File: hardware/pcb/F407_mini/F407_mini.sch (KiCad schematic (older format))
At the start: 37 parts, among them J1 Conn_01x03, J10 Conn_01x03, J11 Conn_01x03, J12 Conn_01x03, J13 Conn_01x03, J14 Conn_01x03, J15 Conn_01x03, J16 Conn_01x03, J17 Conn_01x03, J18 Conn_01x03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

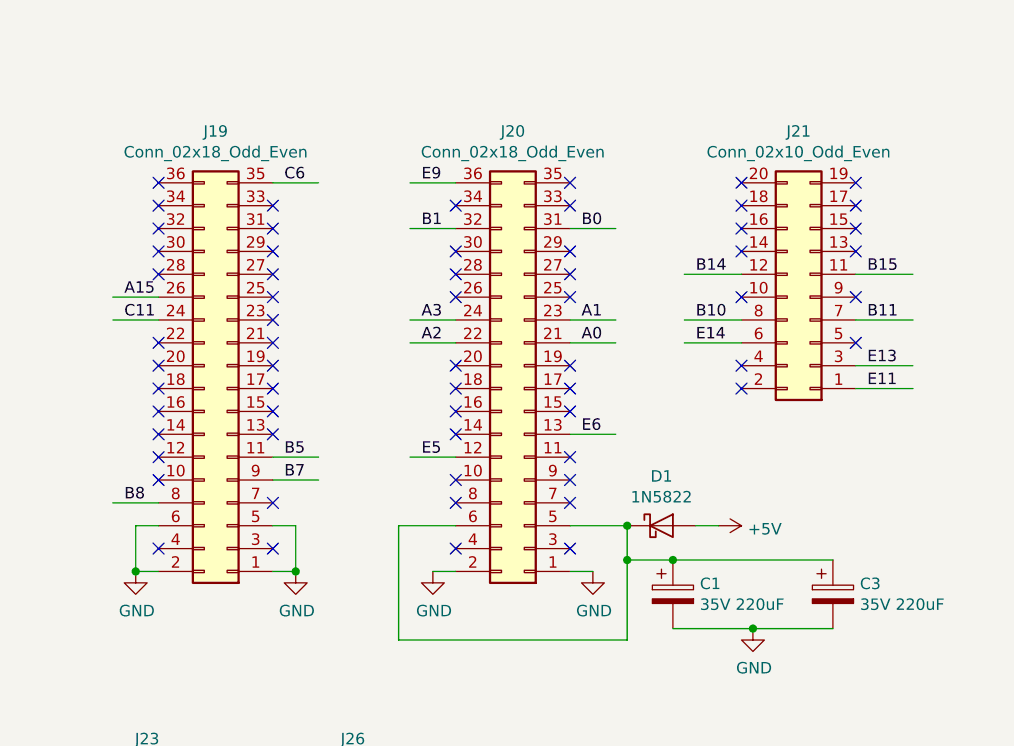
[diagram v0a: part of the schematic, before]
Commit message: flip connectors
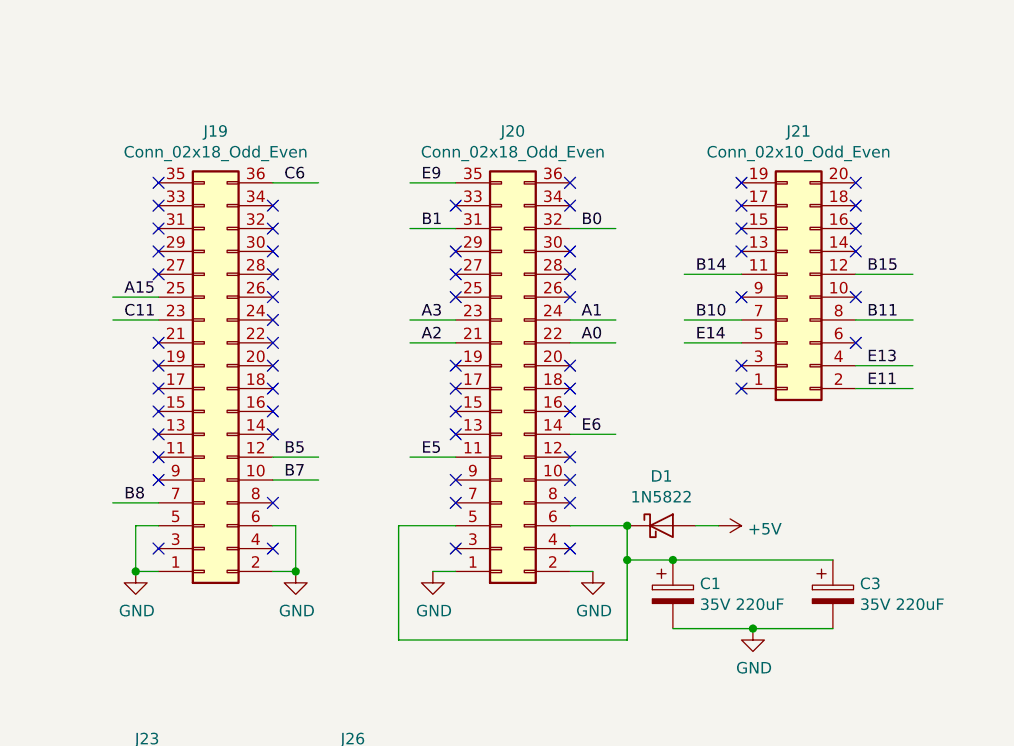
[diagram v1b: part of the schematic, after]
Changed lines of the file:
@@
 L Connector_Generic:Conn_02x10_Odd_Even J21
 U 1 1 5E1B89D1
-P 10000 1950
-F 0 "J21" H 10050 1225 50  0000 C CNN
-F 1 "Conn_02x10_Odd_Even" H 10050 1316 50  0000 C CNN
-F 2 "Connector_PinSocket_2.54mm:PinSocket_2x10_P2.54mm_Vertical" H 10000 1950 50  0001 C CNN
-F 3 "~" H 10000 1950 50  0001 C CNN
-	1    10000 1950
-	-1   0    0    1
+P 9900 1950
+F 0 "J21" H 9950 1225 50  0000 C CNN
+F 1 "Conn_02x10_Odd_Even" H 9950 1316 50  0000 C CNN
+F 2 "Connector_PinSocket_2.54mm:PinSocket_2x10_P2.54mm_Vertical" H 9900 1950 50  0001 C CNN
+F 3 "~" H 9900 1950 50  0001 C CNN
+	1    9900 1950
+	1    0    0    1
 $EndComp
 $Comp
 L Connector_Generic:Conn_02x18_Odd_Even J19
 U 1 1 5E1BA0A2
-P 7450 2350
-F 0 "J19" H 7500 1225 50  0000 C CNN
-F 1 "Conn_02x18_Odd_Even" H 7500 1316 50  0000 C CNN
-F 2 "Connector_PinSocket_2.54mm:PinSocket_2x18_P2.54mm_Vertical" H 7450 2350 50  0001 C CNN
-F 3 "~" H 7450 2350 50  0001 C CNN
-	1    7450 2350
-	-1   0    0    1
+P 7350 2350
+F 0 "J19" H 7400 1225 50  0000 C CNN
+F 1 "Conn_02x18_Odd_Even" H 7400 1316 50  0000 C CNN
+F 2 "Connector_PinSocket_2.54mm:PinSocket_2x18_P2.54mm_Vertical" H 7350 2350 50  0001 C CNN
+F 3 "~" H 7350 2350 50  0001 C CNN
+	1    7350 2350
+	1    0    0    1
 $EndComp
 $Comp
 L Connector_Generic:Conn_02x18_Odd_Even J20
 U 1 1 5E1BD5D3
-P 8750 2350
-F 0 "J20" H 8800 1225 50  0000 C CNN
-F 1 "Conn_02x18_Odd_Even" H 8800 1316 50  0000 C CNN
-F 2 "Connector_PinSocket_2.54mm:PinSocket_2x18_P2.54mm_Vertical" H 8750 2350 50  0001 C CNN
-F 3 "~" H 8750 2350 50  0001 C CNN
-	1    8750 2350
-	-1   0    0    1
+P 8650 2350
+F 0 "J20" H 8700 1225 50  0000 C CNN
+F 1 "Conn_02x18_Odd_Even" H 8700 1316 50  0000 C CNN
+F 2 "Connector_PinSocket_2.54mm:PinSocket_2x18_P2.54mm_Vertical" H 8650 2350 50  0001 C CNN
+F 3 "~" H 8650 2350 50  0001 C CNN
+	1    8650 2350
+	1    0    0    1
 $EndComp
 $Comp

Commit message: F407 mini board RC0
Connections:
- wire segments 107 -> 108
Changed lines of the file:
@@
 EESchema Schematic File Version 4
-LIBS:F407_mini-cache
 EELAYER 30 0
 EELAYER END
@@
 $EndComp
 Wire Wire Line
-	10100 5250 10200 5250
+	10100 5250 10150 5250
 Wire Wire Line
 	10100 5350 10200 5350
@@
 Text Label 8850 4250 0    50   ~ 0
 C11
+$Comp
+L power:PWR_FLAG #FLG0101
+U 1 1 5E7A3214
+P 10150 5250
+F 0 "#FLG0101" H 10150 5325 50  0001 C CNN
+F 1 "PWR_FLAG" H 10150 5423 50  0000 C CNN
+F 2 "" H 10150 5250 50  0001 C CNN
+F 3 "~" H 10150 5250 50  0001 C CNN
+	1    10150 5250
+	1    0    0    -1
+$EndComp
+Connection ~ 10150 5250
+Wire Wire Line
+	10150 5250 10200 5250
+$Comp
+L power:PWR_FLAG #FLG0102
+U 1 1 5E7A3AAC
+P 10200 5350
+F 0 "#FLG0102" H 10200 5425 50  0001 C CNN
+F 1 "PWR_FLAG" H 10200 5523 50  0000 C CNN
+F 2 "" H 10200 5350 50  0001 C CNN
+F 3 "~" H 10200 5350 50  0001 C CNN
+	1    10200 5350
+	-1   0    0    1
+$EndComp
+Connection ~ 10200 5350
 $EndSCHEMATC
